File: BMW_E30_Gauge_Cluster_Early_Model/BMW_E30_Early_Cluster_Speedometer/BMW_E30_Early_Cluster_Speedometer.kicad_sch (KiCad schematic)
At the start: 37 parts, among them J1 Conn_01x06_Socket, J2 Conn_01x04_Socket, M1 Odometer, Q1 BC327-40, Q2 BD135, U1 UAF2115, U2 UGS 3020

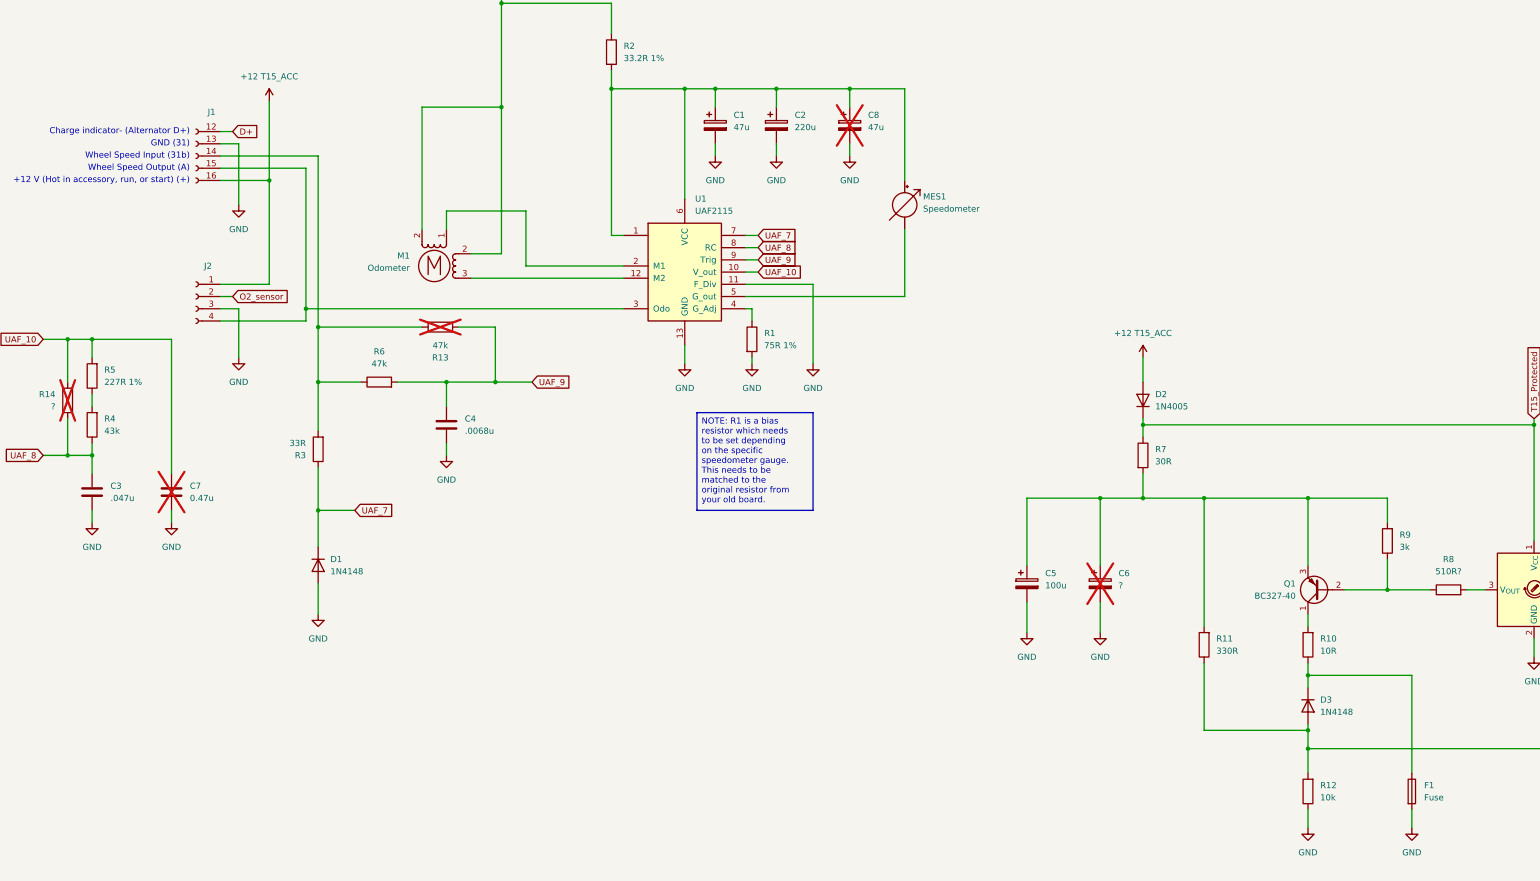
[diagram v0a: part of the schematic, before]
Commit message: Schematic & Layout Changes
Made a few changes to the schematic, changing C2 and C8 connections. Locked in the galvanometer and odometer stepper footprint locations on the board.
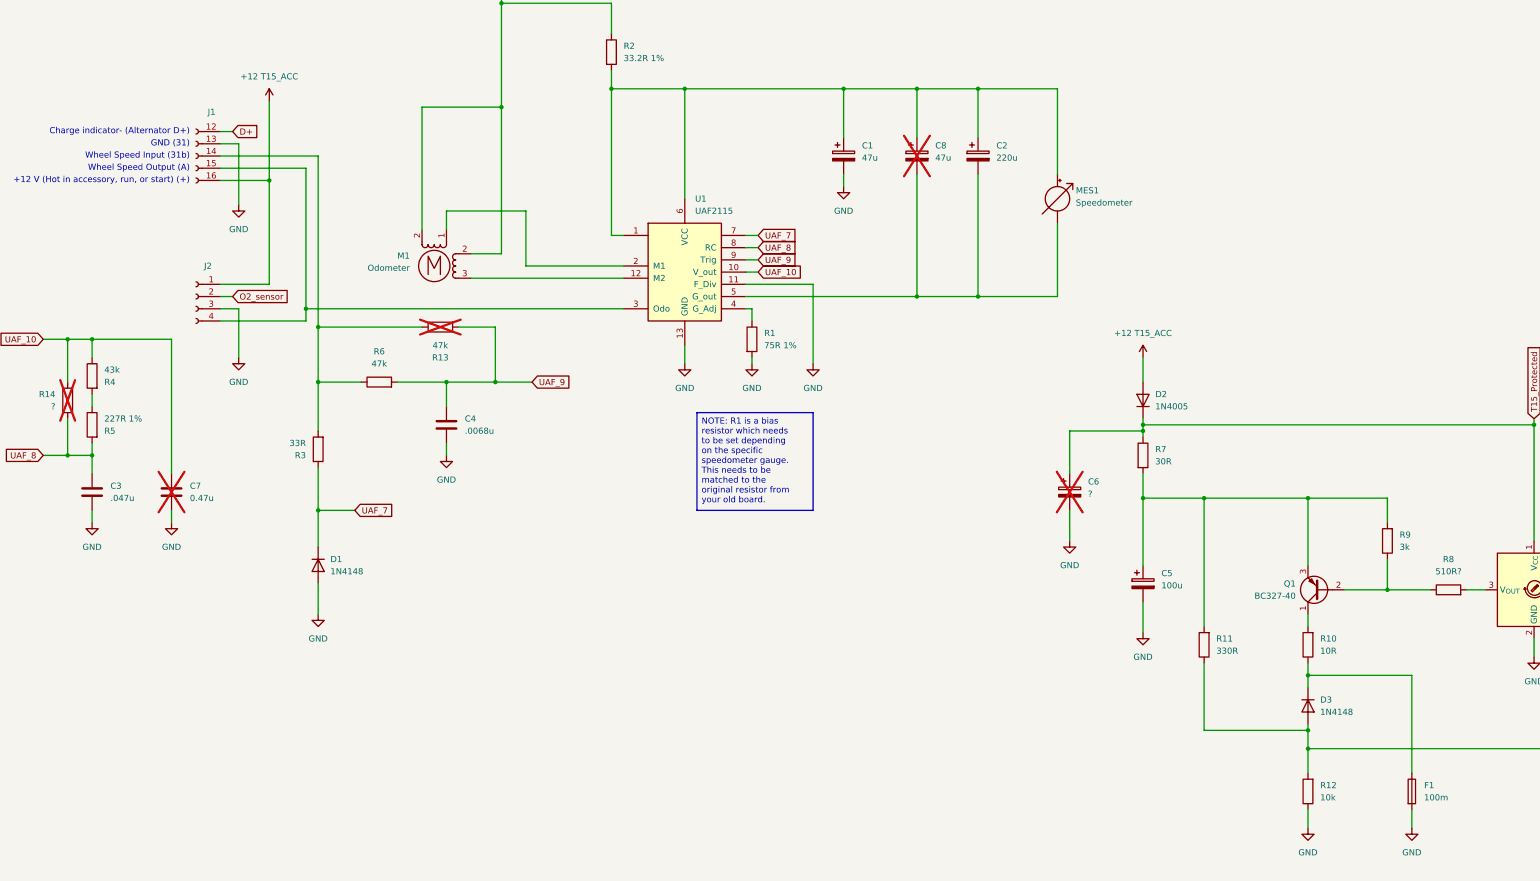
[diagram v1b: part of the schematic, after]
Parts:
- F1: value Fuse -> 100m
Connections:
- net GND: no longer C2.2, C8.2
- net T15_Protected: now also C6.1
- net UAF_10: now also R4.1; no longer R5.2
- net UAF_8: now also R5.2; no longer R4.1
- net at MES1.1 (-), U1.5 (G_out): now also C2.2, C8.2
- net at C5.1, Q1.3 (E), R11.2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: no longer C6.1
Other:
- moved on the sheet: C1, C2, C5, C6, C8, MES1, R4, R5

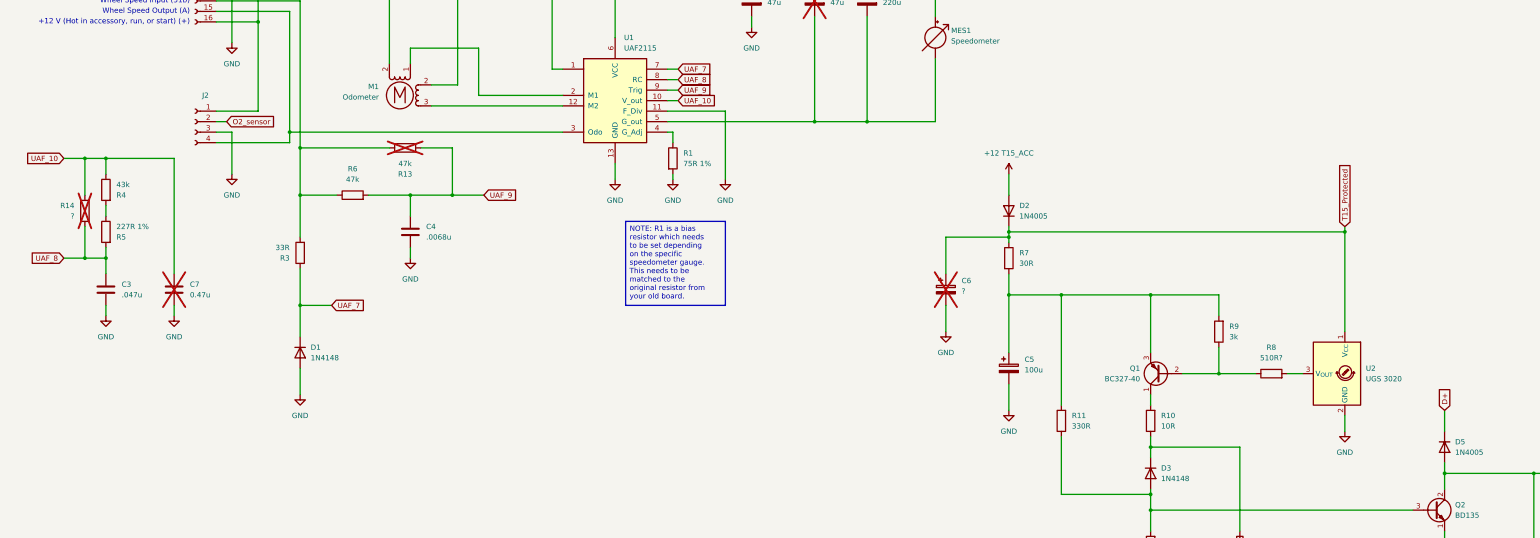
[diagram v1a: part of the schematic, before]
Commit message: Added Hall Sensor Board
Separate board was added for mounting the Hall effect sensor(s) to the main Speedometer board.
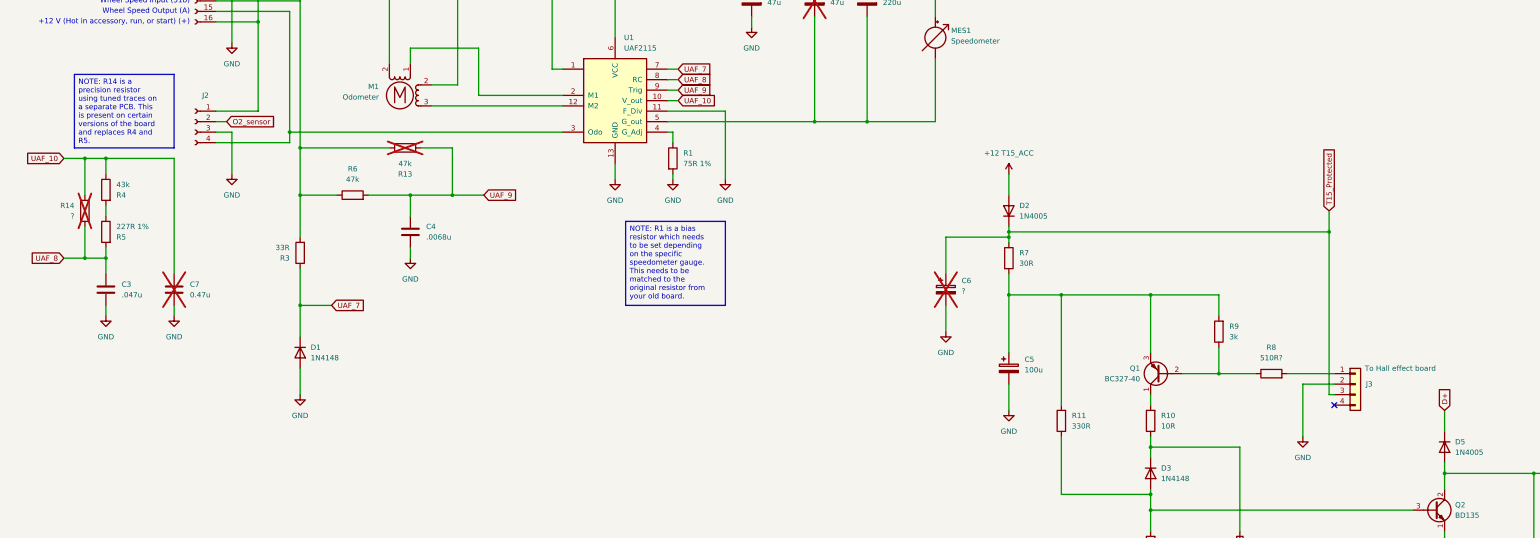
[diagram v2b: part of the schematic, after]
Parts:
- removed U2: UGS 3020, Package_TO_SOT_THT:TO-92S, symbol Sensor_Magnetic:A1302xUA
- added J3: To Hall effect board, Connector_PinHeader_2.54mm:PinHeader_1x04_P2.54mm_Vertical, symbol Connector_Generic:Conn_01x04
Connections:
- net GND: now also J3.2 (Pin_2)
- net T15_Protected: now also J3.3 (Pin_3)
- net at R8.2: now also J3.1 (Pin_1)
- no-connect marks 0 -> 1
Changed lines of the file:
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@@
 		)
 	)
+	(text_box "NOTE: R14 is a precision resistor using tuned traces on a separate PCB. This is present on certain versions of the board and replaces R4 and R5. "
+		(exclude_from_sim no)
+		(at 27.94 78.74 0)
+		(size 24.13 17.78)
+		(margins 0.9525 0.9525 0.9525 0.9525)
+		(stroke
+			(width 0)
+			(type solid)
+		)
+		(fill
+			(type color)
+			(color 255 229 191 1)
+		)
+		(effects
+			(font
+				(size 1.27 1.27)
+			)
+			(justify left top)
+		)
+	)
 	(text_box "NOTE: R1 is a bias resistor which needs to be set depending on the specific speedometer gauge. This needs to be matched to the original resistor from your old board. "
 		(exclude_from_sim no)
@@
 	)
 	(junction
+		(at 331.47 116.84)
+		(diameter 0)
+		(color 0 0 0 0)
+	)
+	(junction
 		(at 288.29 184.15)
 		(diameter 0)
@@
 		(color 0 0 0 0)
 	)
-	(junction
-		(at 335.28 116.84)
-		(diameter 0)
-		(color 0 0 0 0)
+	(no_connect
+		(at 332.74 158.75)
 	)
 	(wire
@@
 	(wire
 		(pts
-			(xy 321.31 151.13) (xy 325.12 151.13)
-		)
-		(stroke
-			(width 0)
-			(type default)
-		)
-	)
-	(wire
-		(pts
 			(xy 288.29 180.34) (xy 288.29 179.07)
 		)
@@
 	(wire
 		(pts
+			(xy 325.12 166.37) (xy 325.12 153.67)
+		)
+		(stroke
+			(width 0)
+			(type default)
+		)
+	)
+	(wire
+		(pts
 			(xy 288.29 180.34) (xy 288.29 184.15)
 		)
@@
 	(wire
 		(pts
+			(xy 325.12 153.67) (xy 332.74 153.67)
+		)
+		(stroke
+			(width 0)
+			(type default)
+		)
+	)
+	(wire
+		(pts
 			(xy 359.41 160.02) (xy 359.41 165.1)
 		)
@@
 	(wire
 		(pts
-			(xy 335.28 116.84) (xy 335.28 140.97)
+			(xy 331.47 156.21) (xy 331.47 116.84)
 		)
 		(stroke
@@
 	(wire
 		(pts
-			(xy 335.28 161.29) (xy 335.28 165.1)
-		)
-		(stroke
-			(width 0)
-			(type default)
-		)
-	)
-	(wire
-		(pts
 			(xy 35.56 113.03) (xy 35.56 110.49)
 		)
@@
 	(wire
 		(pts
-			(xy 254 116.84) (xy 335.28 116.84)
+			(xy 254 116.84) (xy 331.47 116.84)
 		)
 		(stroke
@@
 	(wire
 		(pts
-			(xy 335.28 115.57) (xy 335.28 116.84)
+			(xy 331.47 111.76) (xy 331.47 116.84)
+		)
+		(stroke
+			(width 0)
+			(type default)
+		)
+	)
+	(wire
+		(pts
+			(xy 332.74 156.21) (xy 331.47 156.21)
 		)
 		(stroke
@@
 	(wire
 		(pts
+			(xy 321.31 151.13) (xy 332.74 151.13)
+		)
+		(stroke
+			(width 0)
+			(type default)
+		)
+	)
+	(wire
+		(pts
 			(xy 62.23 55.88) (xy 64.77 55.88)
 		)
@@
 	(global_label "T15_Protected"
 		(shape input)
-		(at 335.28 115.57 90)
+		(at 331.47 111.76 90)
 		(fields_autoplaced yes)
 		(effects
@@
 		)
 		(property "Intersheetrefs" "${INTERSHEET_REFS}"
-			(at 335.28 99.1592 90)
+			(at 331.47 95.3492 90)
 			(effects
 				(font
@@
 	)
 	(symbol
+		(lib_id "Connector_Generic:Conn_01x04")
+		(at 337.82 153.67 0)
+		(unit 1)
+		(exclude_from_sim no)
+		(in_bom yes)
+		(on_board yes)
+		(dnp no)
+		(property "Reference" "J3"
+			(at 340.36 153.6699 0)
+			(effects
+				(font
+					(size 1.27 1.27)
+				)
+				(justify left)
+			)
+		)
+		(property "Value" "To Hall effect board"
+			(at 340.106 149.86 0)
+			(effects
+				(font
+					(size 1.27 1.27)
+				)
+				(justify left)
+			)
+		)
+		(property "Footprint" "Connector_PinHeader_2.54mm:PinHeader_1x04_P2.54mm_Vertical"
+			(at 337.82 153.67 0)
+			(effects
+				(font
+					(size 1.27 1.27)
+				)
+				(hide yes)
+			)
+		)
+		(property "Datasheet" "~"
+			(at 337.82 153.67 0)
+			(effects
+				(font
+					(size 1.27 1.27)
+				)
+				(hide yes)
+			)
+		)
+		(property "Description" "Generic connector, single row, 01x04, script generated (kicad-library-utils/schlib/autogen/connector/)"
+			(at 337.82 153.67 0)
+			(effects
+				(font
+					(size 1.27 1.27)
+				)
+				(hide yes)
+			)
+		)
+		(pin "3"
+		)
+		(pin "2"
+		)
+		(pin "1"
+		)
+		(pin "4"
+		)
+		(instances
+			(project ""
+				(path "/9a835706-2a71-4b4d-aadf-5c5569044960"
+					(reference "J3")
+					(unit 1)
+				)
+			)
+		)
+	)
+	(symbol
 		(lib_id "Device:R")
 		(at 288.29 193.04 180)
@@
 	)
 	(symbol
-		(lib_id "power:GND")
-		(at 335.28 165.1 0)
-		(unit 1)
-		(exclude_from_sim no)
-		(in_bom yes)
-		(on_board yes)
-		(dnp no)
-		(property "Reference" "#PWR016"
-			(at 335.28 171.45 0)
-			(effects
-				(font
-					(size 1.27 1.27)
-				)
-				(hide yes)
-			)
-		)
-		(property "Value" "GND"
-			(at 335.28 170.18 0)
-			(effects
-				(font
-					(size 1.27 1.27)
-				)
-			)
-		)
-		(property "Footprint" ""
-			(at 335.28 165.1 0)
-			(effects
-				(font
-					(size 1.27 1.27)
-				)
-				(hide yes)
-			)
-		)
-		(property "Datasheet" ""
-			(at 335.28 165.1 0)
-			(effects
-				(font
-					(size 1.27 1.27)
-				)
-				(hide yes)
-			)
-		)
-		(property "Description" "Power symbol creates a global label with name \"GND\" , ground"
-			(at 335.28 165.1 0)
-			(effects
-				(font
-					(size 1.27 1.27)
-				)
-				(hide yes)
-			)
-		)
-		(pin "1"
-		)
-		(instances
-			(project "BMW_E30_Early_Cluster_Speedometer"
-				(path "/9a835706-2a71-4b4d-aadf-5c5569044960"
-					(reference "#PWR016")
-					(unit 1)
-				)
-			)
-		)
-	)
-	(symbol
 		(lib_id "Device:R")
 		(at 35.56 106.68 0)
@@
 	)
 	(symbol
-		(lib_id "Sensor_Magnetic:A1302xUA")
-		(at 332.74 151.13 0)
-		(mirror y)
-		(unit 1)
-		(exclude_from_sim no)
-		(in_bom yes)
-		(on_board yes)
-		(dnp no)
-		(property "Reference" "U2"
-			(at 340.36 149.8599 0)
-			(effects
-				(font
-					(size 1.27 1.27)
-				)
-				(justify right)
-			)
-		)
-		(property "Value" "UGS 3020"
-			(at 340.36 152.3999 0)
-			(effects
-				(font
-					(size 1.27 1.27)
-				)
-				(justify right)
-			)
-		)
-		(property "Footprint" "Package_TO_SOT_THT:TO-92S"
-			(at 332.74 168.148 0)
-			(effects
-				(font
-					(size 1.27 1.27)
-					(italic yes)
-				)
-				(hide yes)
-			)
-		)
-		(property "Datasheet" ""
-			(at 332.74 164.084 0)
-			(effects
-				(font
-					(size 1.27 1.27)
-				)
-				(hide yes)
-			)
-		)
-		(property "Description" ""
-			(at 332.74 166.116 0)
-			(effects
-				(font
-					(size 1.27 1.27)
-				)
-				(hide yes)
-			)
-		)
-		(pin "3"
-		)
-		(pin "1"
-		)
-		(pin "2"
-		)
-		(instances
-			(project ""
-				(path "/9a835706-2a71-4b4d-aadf-5c5569044960"
-					(reference "U2")
-					(unit 1)
-				)
-			)
-		)
-	)
-	(symbol
 		(lib_id "power:GND")
 		(at 52.07 137.16 0)
@@
 					(unit 1)
 				)
+			)
+		)
+	)
+	(symbol
+		(lib_id "power:GND")
+		(at 325.12 166.37 0)
+		(unit 1)
+		(exclude_from_sim no)
+		(in_bom yes)
+		(on_board yes)
+		(dnp no)
+		(property "Reference" "#PWR08"
+			(at 325.12 172.72 0)
+			(effects
+				(font
+					(size 1.27 1.27)
+				)
+				(hide yes)
+			)
+		)
+		(property "Value" "GND"
+			(at 325.12 171.45 0)
+			(effects
+				(font
+					(size 1.27 1.27)
+				)
+			)
+		)
+		(property "Footprint" ""
+			(at 325.12 166.37 0)
+			(effects
+				(font
+					(size 1.27 1.27)
+				)
+				(hide yes)
+			)
+		)
+		(property "Datasheet" ""
+			(at 325.12 166.37 0)
+			(effects
+				(font
+					(size 1.27 1.27)
+				)
+				(hide yes)
+			)
+		)
+		(property "Description" "Power symbol creates a global label with name \"GND\" , ground"
+			(at 325.12 166.37 0)
+			(effects
+				(font
+					(size 1.27 1.27)
+				)
+				(hide yes)
+			)
+		)
+		(pin "1"
+		)
+		(instances
+			(project "BMW_E30_Early_Cluster_Speedometer"
+				(path "/9a835706-2a71-4b4d-aadf-5c5569044960"
+					(reference "#PWR08")
+					(unit 1)
+				)
